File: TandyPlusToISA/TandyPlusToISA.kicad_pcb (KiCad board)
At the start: 2 copper layers, 83.6 x 12.7 mm, 2 parts, among them J1 Bus_ISA_8bit, J3 TANDY PLUS HEADER

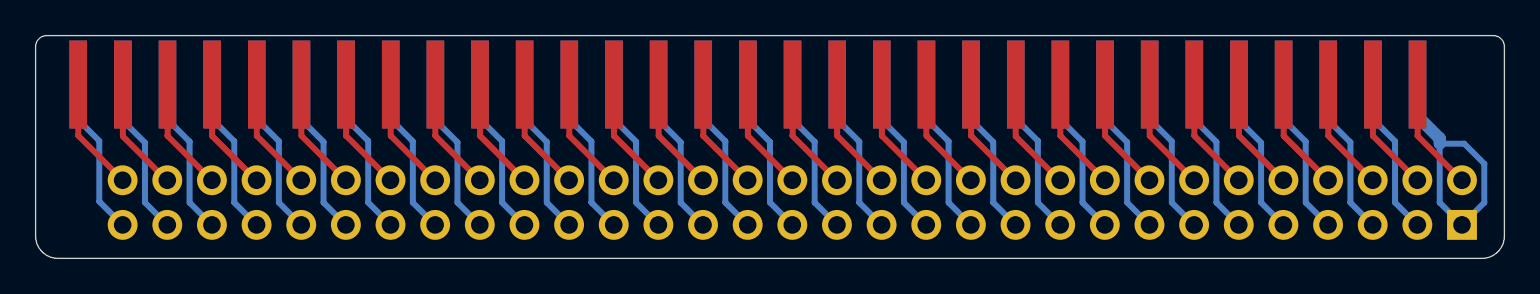
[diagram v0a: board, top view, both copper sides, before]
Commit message: Shifted Plus to ISA adapters a little, updated tested status
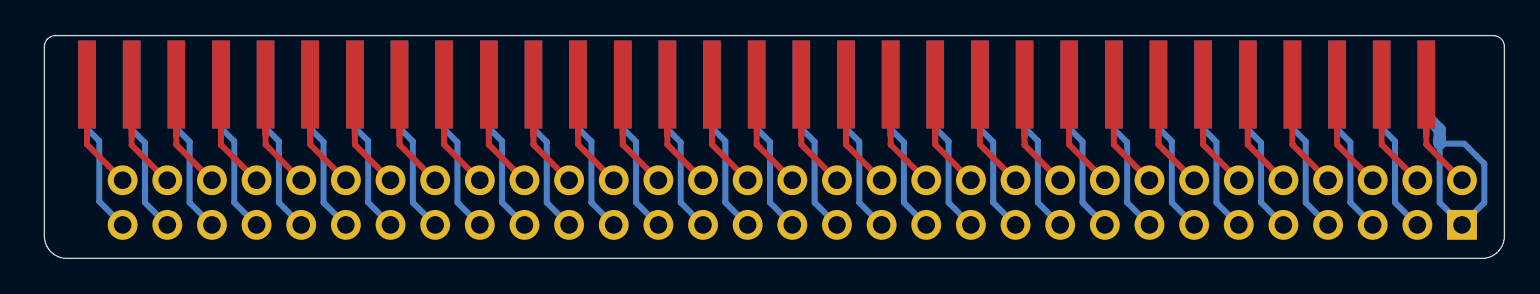
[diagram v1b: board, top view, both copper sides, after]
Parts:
- moved J1 0.50 mm to (173.2, 110.1)
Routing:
- net IOCHRDY: track 6.55 -> 7.18 mm
- net A01: track 6.52 -> 7.15 mm
- net A03: track 6.53 -> 7.14 mm
- net A02: track 6.52 -> 7.13 mm
- net A12: track 6.51 -> 7.12 mm
- net A11: track 6.51 -> 7.11 mm
- net A10: track 6.53 -> 7.13 mm
- net A09: track 6.50 -> 7.10 mm
- net A08: track 6.52 -> 7.13 mm
- net A07: track 6.51 -> 7.12 mm
- net A06: track 6.50 -> 7.11 mm
- net A04: track 6.53 -> 7.14 mm
- net AEN: track 6.51 -> 7.11 mm
- net A19: track 6.51 -> 7.11 mm
- net A18: track 6.52 -> 7.13 mm
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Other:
- board size 83.6 x 12.7 mm -> 83.1 x 12.7 mm
